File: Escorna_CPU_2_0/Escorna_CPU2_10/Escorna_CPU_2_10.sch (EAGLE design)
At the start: 75 parts, among them IC1 ULN2803, U2 ESP01, X1 AK550/2, X1.1 AK550/2

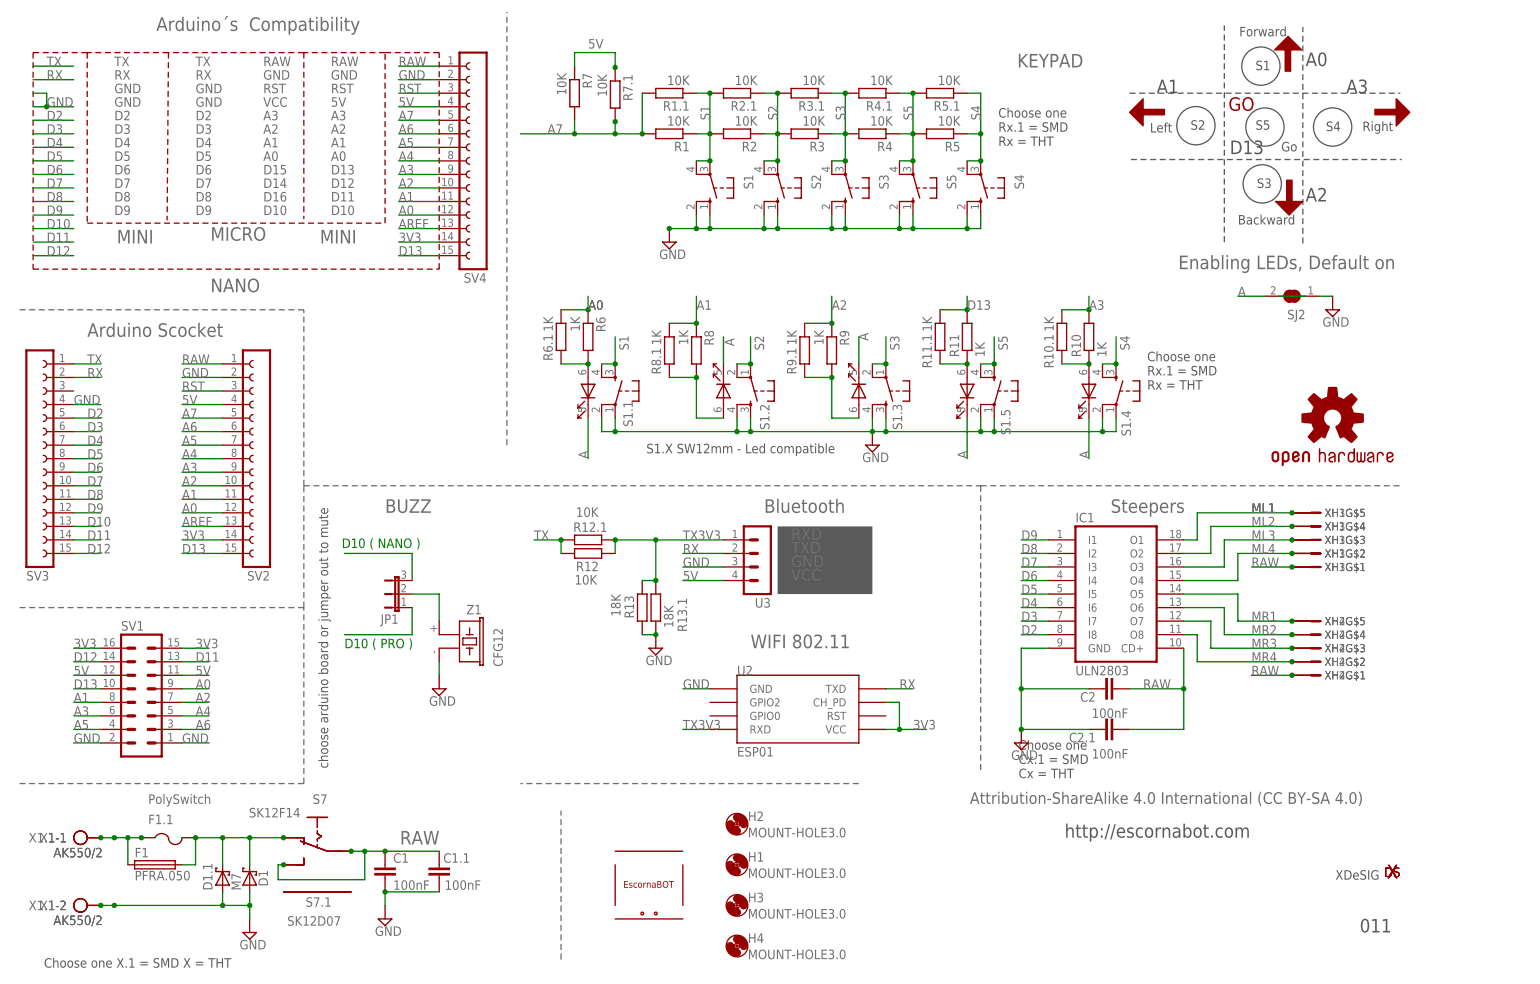
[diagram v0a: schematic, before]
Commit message: new values
New values of resistors, (R5) for the switch S5 and (R10) improves the
brightness of the green LED.
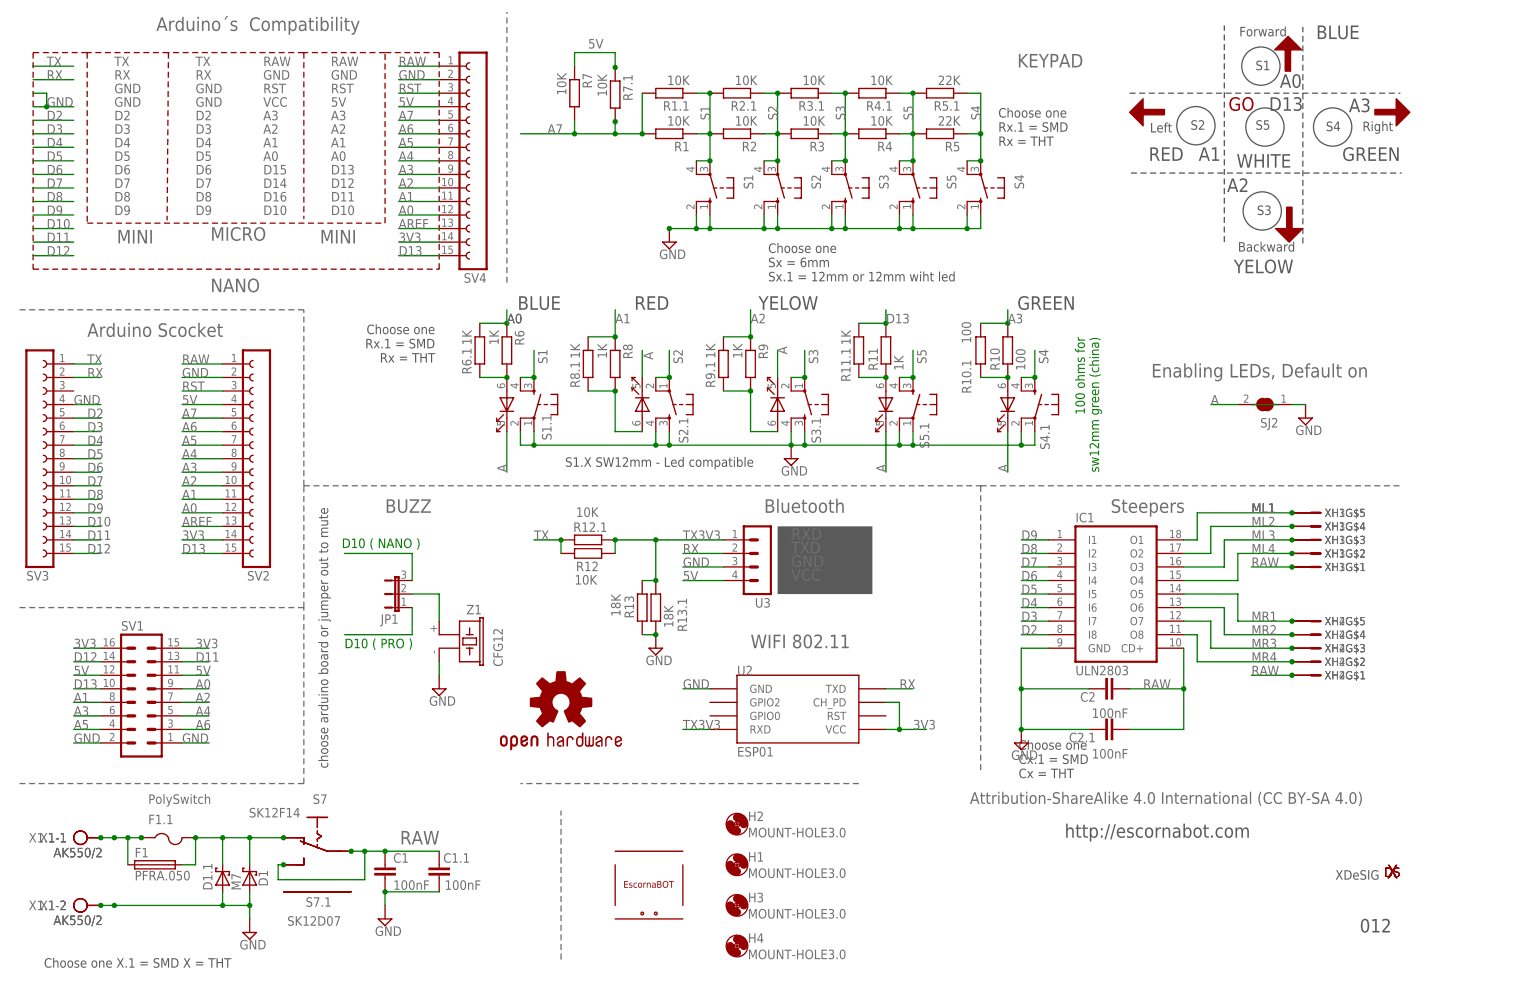
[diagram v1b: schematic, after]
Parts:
- removed S1.2, S1.3, S1.4, S1.5: B3F-9XXX, Escorna_CPU_2_01:SWITCH-OMRON_B3F-9XXX
- added S2.1, S3.1, S4.1, S5.1: B3F-9XXX, Escorna_CPU_2_01:SWITCH-OMRON_B3F-9XXX
- R10, R10.1: value 1K -> 100
- R5, R5.1: value 10K -> 22K
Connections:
- net A: now also S2.1.K, S3.1.K, S4.1.K, S5.1.K; no longer S1.2.K, S1.3.K, S1.4.K, S1.5.K
- net GND: now also S2.1.S, S2.1.S1, S3.1.S, S3.1.S1, S4.1.P, S4.1.P1, S5.1.P, S5.1.P1; no longer S1.2.S, S1.2.S1, S1.3.S, S1.3.S1, S1.4.P, S1.4.P1, S1.5.P, S1.5.P1
- net N$13: now also S5.1.A; no longer S1.5.A
- net N$4: now also S2.1.A; no longer S1.2.A
- net N$6: now also S3.1.A; no longer S1.3.A
- net N$8: now also S4.1.A; no longer S1.4.A
- net S2: now also S2.1.P, S2.1.P1; no longer S1.2.P, S1.2.P1
- net S3: now also S3.1.P, S3.1.P1; no longer S1.3.P, S1.3.P1
- net S4: now also S4.1.S, S4.1.S1; no longer S1.4.S, S1.4.S1
- net S5: now also S5.1.S, S5.1.S1; no longer S1.5.S, S1.5.S1
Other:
- note added: "012"
- note added: "100 ohms for sw12mm green (china)"
- note added: "BLUE"
- note added: "Choose one Sx = 6mm Sx.1 = 12mm or 12mm wiht led"
- note added: "GREEN"
- note added: "RED"
- note added: "WHITE"
- note added: "YELOW"
- note removed: "011"
- note removed: "Go"
- moved on the sheet: R10, R10.1, R11, R11.1, R6, R6.1, R8, R8.1, R9, R9.1, S1.1, SJ2
